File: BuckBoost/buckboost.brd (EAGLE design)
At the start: 100.1 x 80.4 mm, 10 parts

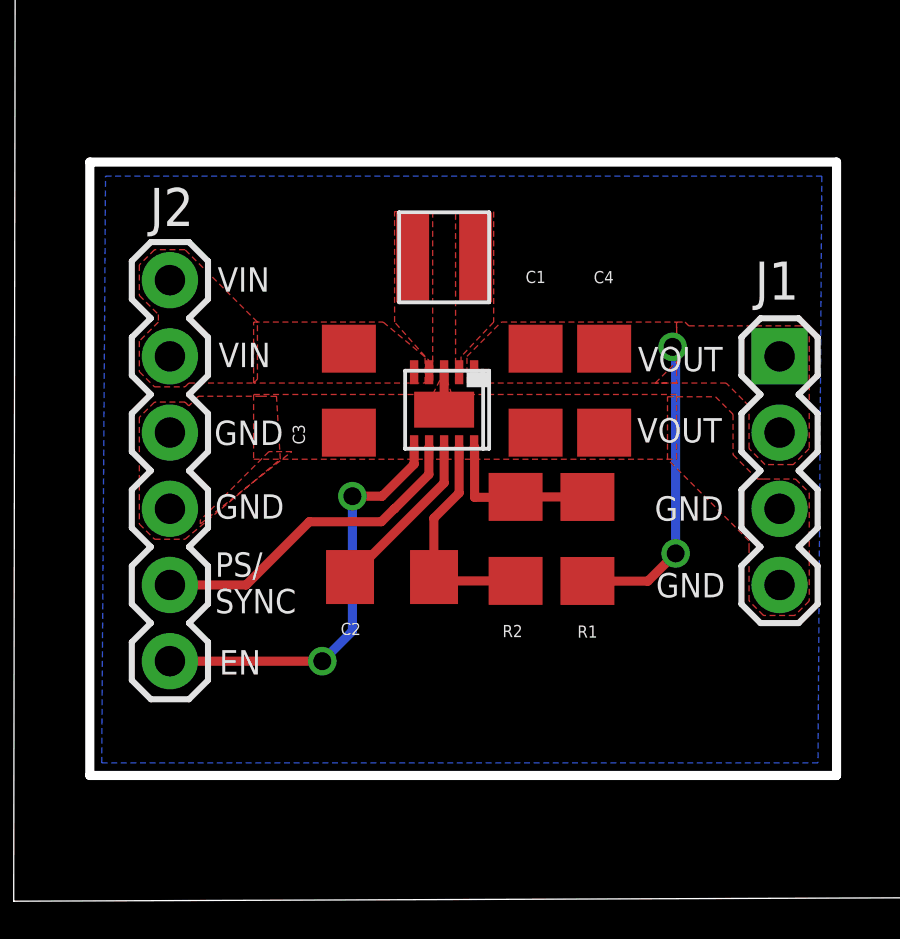
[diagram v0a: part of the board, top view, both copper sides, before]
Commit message: Added Jumpers
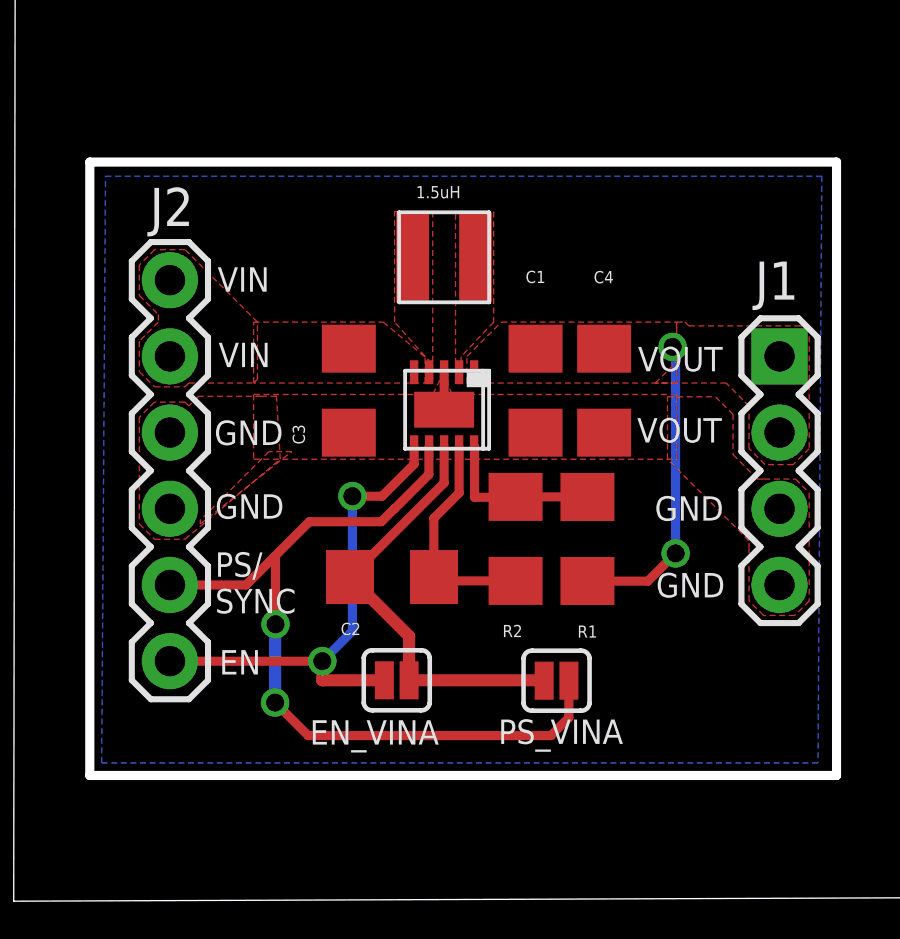
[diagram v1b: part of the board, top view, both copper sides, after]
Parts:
- added SJ1, SJ2: SOLDERJUMPERNC, SparkFun-Retired:SJ_2S
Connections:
- removed net N$2: J2.1, U$1.6
- new net N$5: J2.1, SJ1.1, U$1.6
- net N$3: now also SJ1.2, SJ2.1
- net N$4: now also SJ2.2
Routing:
- net N$5: track 0.00 -> 16.8 mm, vias 0 -> 2
- net N$4: track 11.1 -> 27.7 mm, vias 0 -> 2
- net N$2: track 14.1 -> 0.00 mm, vias 2 -> 0
- net N$3: track 5.63 -> 14.4 mm
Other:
- board text added: "1.5uH"
- board text added: "EN_VINA"
- board text added: "PS_VINA"
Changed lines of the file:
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@@
 <text x="21.236940625" y="12.303759375" size="0.8128" layer="21">GND</text>
 <text x="21.282659375" y="9.74598125" size="0.8128" layer="21">GND</text>
+<text x="9.743440625" y="4.8387" size="0.8128" layer="21">EN_VINA</text>
+<text x="16.024859375" y="4.861559375" size="0.8128" layer="21">PS_VINA</text>
+<text x="13.27911875" y="23.0505" size="0.4064" layer="21">1.5uH</text>
 </plain>
 <attributes>
@@
 <attribute name="VALUE" x="8.255" y="6.35" size="1.27" layer="27" rot="R90"/>
 </element>
+<element name="SJ1" library="SparkFun-Retired" package="SJ_2S" value="SOLDERJUMPERNC" x="12.64158125" y="6.982465625" smashed="yes"/>
+<element name="SJ2" library="SparkFun-Retired" package="SJ_2S" value="SOLDERJUMPERNC" x="17.9679625" y="6.969759375" smashed="yes"/>
 </elements>
 <signals>
@@
 <wire x1="14.22035625" y1="14.752" x2="14.22035625" y2="13.56035625" width="0.3048" layer="1"/>
 <wire x1="14.22035625" y1="13.56035625" x2="11.083778125" y2="10.423778125" width="0.3048" layer="1"/>
+<contactref element="SJ2" pad="1"/>
+<contactref element="SJ1" pad="2"/>
+<wire x1="13.05348125" y1="6.982465625" x2="13.05348125" y2="8.454075" width="0.4064" layer="1"/>
+<wire x1="13.05348125" y1="8.454075" x2="11.083778125" y2="10.423778125" width="0.4064" layer="1"/>
+<wire x1="13.05348125" y1="6.982465625" x2="17.54335625" y2="6.982465625" width="0.4064" layer="1"/>
+<wire x1="17.54335625" y1="6.982465625" x2="17.5560625" y2="6.969759375" width="0.4064" layer="1"/>
 </signal>
 <signal name="L2">
@@
 </polygon>
 </signal>
-<signal name="N$2">
+<signal name="N$4">
+<contactref element="U$1" pad="7"/>
+<wire x1="12.56935625" y1="12.7" x2="13.71235625" y2="13.843" width="0.3048" layer="1"/>
+<wire x1="13.71235625" y1="13.843" x2="13.71235625" y2="14.744" width="0.3048" layer="1"/>
+<wire x1="13.71235625" y1="14.744" x2="13.72035625" y2="14.752" width="0.3048" layer="1"/>
+<contactref element="J2" pad="2"/>
+<wire x1="5.08" y1="10.16" x2="7.62" y2="10.16" width="0.3048" layer="1"/>
+<wire x1="12.56935625" y1="12.7" x2="12.5603" y2="12.7" width="0.3048" layer="1"/>
+<wire x1="12.5603" y1="12.7" x2="12.1285" y2="12.2682" width="0.3048" layer="1"/>
+<wire x1="12.1285" y1="12.2682" x2="9.7282" y2="12.2682" width="0.3048" layer="1"/>
+<wire x1="9.7282" y1="12.2682" x2="8.569959375" y2="11.109959375" width="0.3048" layer="1"/>
+<contactref element="SJ2" pad="2"/>
+<via x="8.5877375" y="6.240778125" extent="1-16" drill="0.6" shape="square"/>
+<via x="8.60044375" y="8.849359375" extent="1-16" drill="0.6" shape="square"/>
+<wire x1="8.569959375" y1="11.109959375" x2="7.62" y2="10.16" width="0.3048" layer="1"/>
+<wire x1="8.5877375" y1="6.240778125" x2="8.5877375" y2="8.836653125" width="0.4064" layer="16"/>
+<wire x1="8.5877375" y1="8.836653125" x2="8.60044375" y2="8.849359375" width="0.4064" layer="16"/>
+<wire x1="8.60044375" y1="8.849359375" x2="8.60044375" y2="11.079475" width="0.3048" layer="1"/>
+<wire x1="8.60044375" y1="11.079475" x2="8.569959375" y2="11.109959375" width="0.3048" layer="1"/>
+<wire x1="18.3798625" y1="6.969759375" x2="18.3798625" y2="5.73828125" width="0.3048" layer="1"/>
+<wire x1="18.3798625" y1="5.73828125" x2="17.78" y2="5.13841875" width="0.3048" layer="1"/>
+<wire x1="17.78" y1="5.13841875" x2="9.690096875" y2="5.13841875" width="0.3048" layer="1"/>
+<wire x1="9.690096875" y1="5.13841875" x2="8.5877375" y2="6.240778125" width="0.3048" layer="1"/>
+</signal>
+<signal name="N$5">
+<contactref element="SJ1" pad="1"/>
 <contactref element="U$1" pad="6"/>
 <contactref element="J2" pad="1"/>
@@
 <via x="10.16" y="7.62" extent="1-16" drill="0.6" shape="square"/>
 <wire x1="10.16" y1="7.62" x2="5.08" y2="7.62" width="0.3048" layer="1"/>
-</signal>
-<signal name="N$4">
-<contactref element="U$1" pad="7"/>
-<wire x1="12.56935625" y1="12.7" x2="13.71235625" y2="13.843" width="0.3048" layer="1"/>
-<wire x1="13.71235625" y1="13.843" x2="13.71235625" y2="14.744" width="0.3048" layer="1"/>
-<wire x1="13.71235625" y1="14.744" x2="13.72035625" y2="14.752" width="0.3048" layer="1"/>
-<contactref element="J2" pad="2"/>
-<wire x1="5.08" y1="10.16" x2="7.62" y2="10.16" width="0.3048" layer="1"/>
-<wire x1="12.56935625" y1="12.7" x2="12.5603" y2="12.7" width="0.3048" layer="1"/>
-<wire x1="12.5603" y1="12.7" x2="12.1285" y2="12.2682" width="0.3048" layer="1"/>
-<wire x1="12.1285" y1="12.2682" x2="9.7282" y2="12.2682" width="0.3048" layer="1"/>
-<wire x1="9.7282" y1="12.2682" x2="7.62" y2="10.16" width="0.3048" layer="1"/>
+<wire x1="12.22968125" y1="6.982465625" x2="10.16" y2="6.982465625" width="0.4064" layer="1"/>
+<wire x1="10.16" y1="6.982465625" x2="10.16" y2="7.62" width="0.4064" layer="1"/>
 </signal>
 </signals>

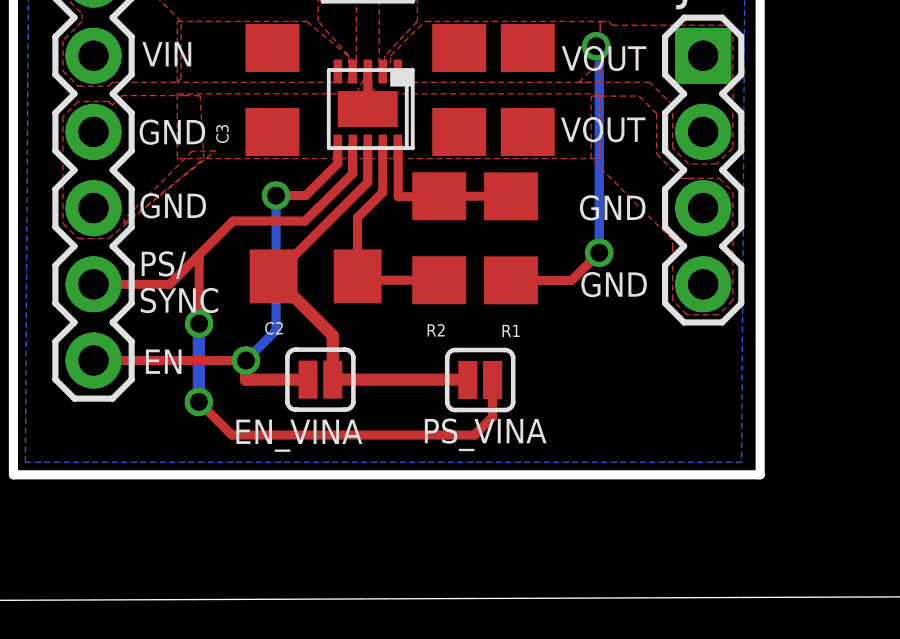
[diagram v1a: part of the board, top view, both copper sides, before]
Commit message: Added vout_vfb jumper
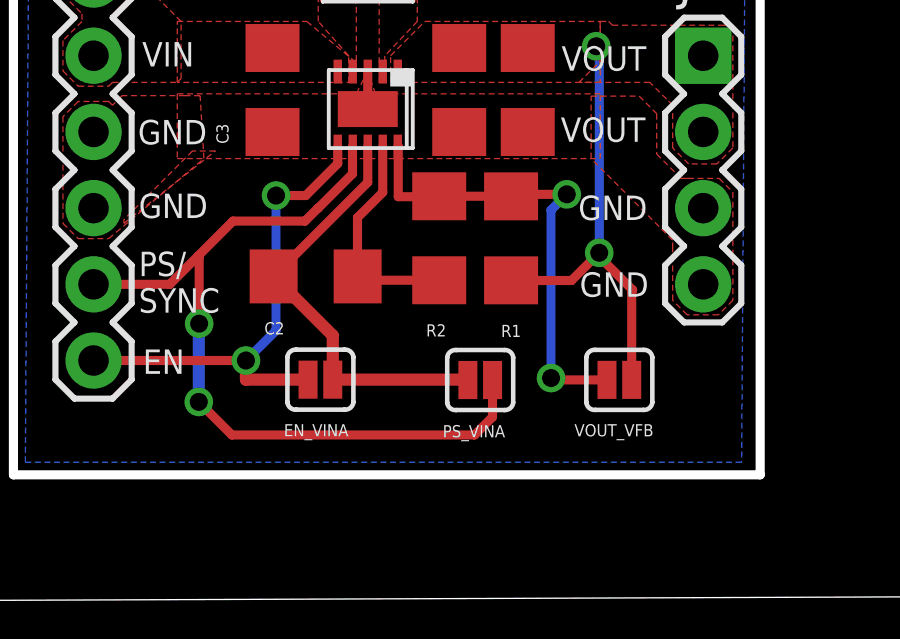
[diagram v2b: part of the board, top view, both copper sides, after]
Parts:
- added SJ3: SOLDERJUMPERNC, SparkFun-Retired:SJ_2S
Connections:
- net N$1: now also SJ3.1
- net VOUT: now also SJ3.2
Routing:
- net N$1: track 5.46 -> 15.6 mm, vias 0 -> 2
- net VOUT: track 10.3 -> 15.0 mm
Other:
- board text added: "VOUT_VFB"
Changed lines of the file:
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@@
 <text x="21.236940625" y="12.303759375" size="0.8128" layer="21">GND</text>
 <text x="21.282659375" y="9.74598125" size="0.8128" layer="21">GND</text>
-<text x="9.743440625" y="4.8387" size="0.8128" layer="21">EN_VINA</text>
-<text x="16.024859375" y="4.861559375" size="0.8128" layer="21">PS_VINA</text>
 <text x="13.27911875" y="23.0505" size="0.4064" layer="21">1.5uH</text>
+<text x="11.42491875" y="5.0927" size="0.4064" layer="21">EN_VINA</text>
+<text x="16.71828125" y="5.05968125" size="0.4064" layer="21">PS_VINA</text>
+<text x="21.1074" y="5.0927" size="0.4064" layer="21">VOUT_VFB</text>
 </plain>
 <attributes>
@@
 <element name="SJ1" library="SparkFun-Retired" package="SJ_2S" value="SOLDERJUMPERNC" x="12.64158125" y="6.982465625" smashed="yes"/>
 <element name="SJ2" library="SparkFun-Retired" package="SJ_2S" value="SOLDERJUMPERNC" x="17.9679625" y="6.969759375" smashed="yes"/>
+<element name="SJ3" library="SparkFun-Retired" package="SJ_2S" value="SOLDERJUMPERNC" x="22.606" y="6.974840625" smashed="yes"/>
 </elements>
 <signals>
@@
 <wire x1="21.93678125" y1="11.211690625" x2="21.93678125" y2="17.9960375" width="0.3048" layer="16"/>
 <wire x1="21.93678125" y1="17.9960375" x2="21.8369375" y2="18.09588125" width="0.3048" layer="16"/>
+<contactref element="SJ3" pad="2"/>
+<wire x1="23.05091875" y1="9.96908125" x2="21.93678125" y2="11.08321875" width="0.3048" layer="1"/>
+<wire x1="21.93678125" y1="11.08321875" x2="21.93678125" y2="11.211690625" width="0.3048" layer="1"/>
+<wire x1="23.05091875" y1="9.96908125" x2="23.0179" y2="9.9360625" width="0.3048" layer="1"/>
+<wire x1="23.0179" y1="9.9360625" x2="23.0179" y2="6.974840625" width="0.3048" layer="1"/>
 </signal>
 <signal name="N$1">
@@
 <wire x1="15.23635625" y1="13.081" x2="16.60293125" y2="13.081" width="0.3048" layer="1"/>
 <wire x1="16.60293125" y1="13.081" x2="16.60293125" y2="13.0957" width="0.3048" layer="1"/>
+<contactref element="SJ3" pad="1"/>
+<wire x1="18.99775625" y1="13.0930875" x2="19.064409375" y2="13.159740625" width="0.3048" layer="1"/>
+<wire x1="19.064409375" y1="13.159740625" x2="20.8534" y2="13.159740625" width="0.3048" layer="1"/>
+<via x="20.8534" y="13.159740625" extent="1-16" drill="0.6" shape="square"/>
+<wire x1="20.8534" y1="13.159740625" x2="20.330159375" y2="12.6365" width="0.3048" layer="16"/>
+<wire x1="20.330159375" y1="12.6365" x2="20.330159375" y2="7.0358" width="0.3048" layer="16"/>
+<via x="20.330159375" y="7.0358" extent="1-16" drill="0.6" shape="square"/>
+<wire x1="20.330159375" y1="7.0358" x2="20.39111875" y2="6.974840625" width="0.3048" layer="1"/>
+<wire x1="20.39111875" y1="6.974840625" x2="22.1941" y2="6.974840625" width="0.3048" layer="1"/>
 </signal>
 <signal name="GND">

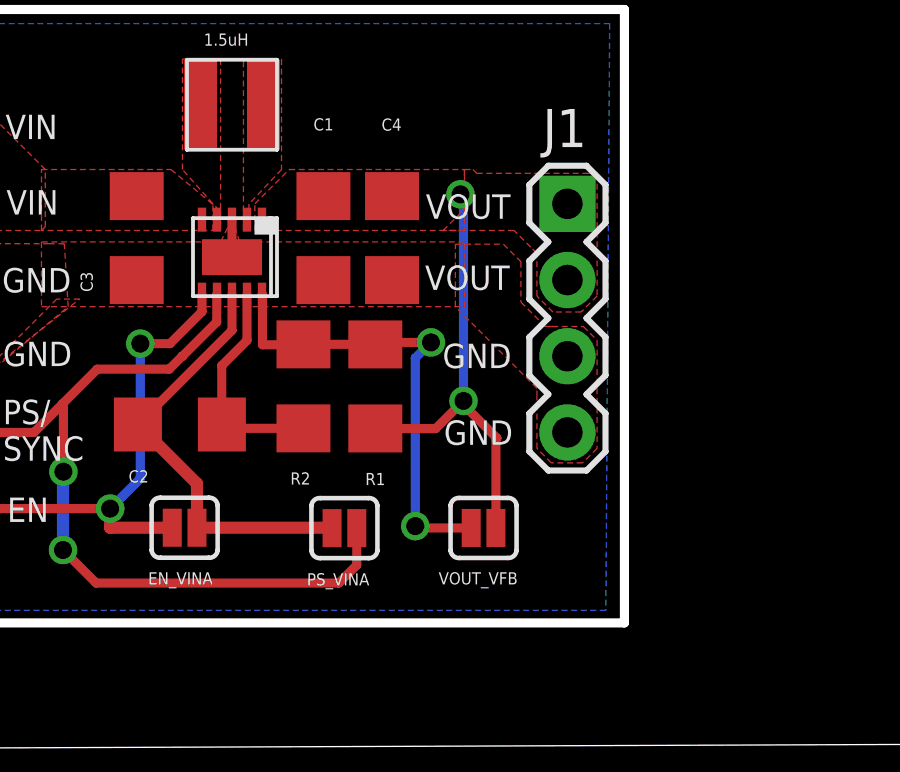
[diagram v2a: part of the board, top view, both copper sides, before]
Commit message: moved fb_vout jumper
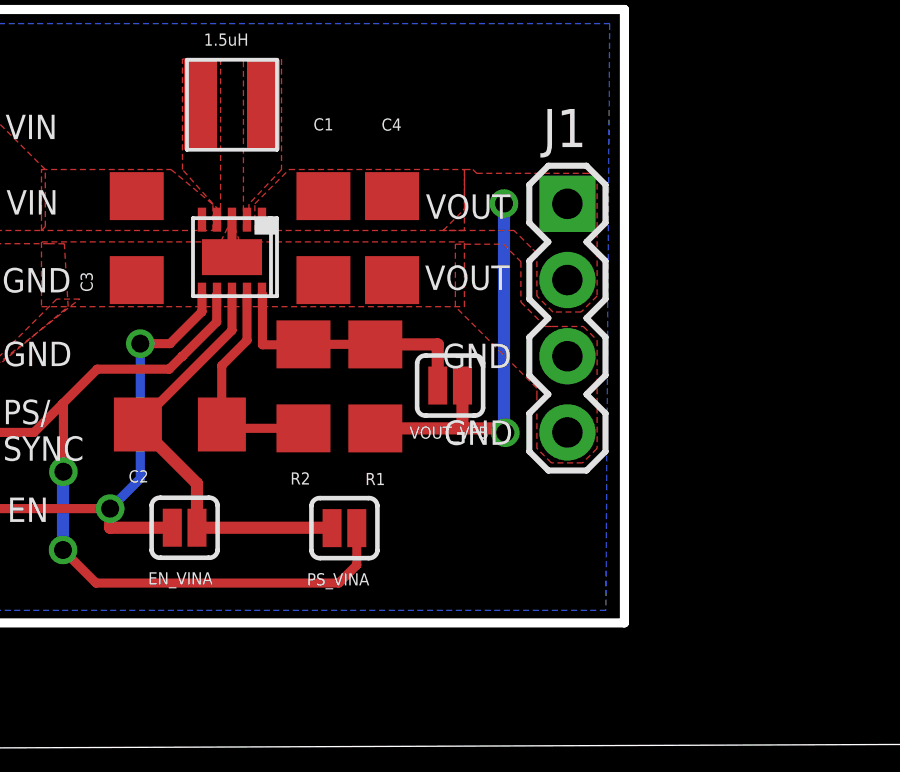
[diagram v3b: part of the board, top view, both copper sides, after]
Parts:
- moved SJ3 4.88 mm to (21.5, 11.7)
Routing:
- net N$1: track 15.6 -> 9.01 mm, vias 2 -> 0
- net VOUT: track 15.0 -> 13.6 mm
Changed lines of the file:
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@@
 <text x="11.42491875" y="5.0927" size="0.4064" layer="21">EN_VINA</text>
 <text x="16.71828125" y="5.05968125" size="0.4064" layer="21">PS_VINA</text>
-<text x="21.1074" y="5.0927" size="0.4064" layer="21">VOUT_VFB</text>
+<text x="20.13711875" y="9.94918125" size="0.4064" layer="21">VOUT_VFB</text>
 </plain>
 <attributes>
@@
 <element name="SJ1" library="SparkFun-Retired" package="SJ_2S" value="SOLDERJUMPERNC" x="12.64158125" y="6.982465625" smashed="yes"/>
 <element name="SJ2" library="SparkFun-Retired" package="SJ_2S" value="SOLDERJUMPERNC" x="17.9679625" y="6.969759375" smashed="yes"/>
-<element name="SJ3" library="SparkFun-Retired" package="SJ_2S" value="SOLDERJUMPERNC" x="22.606" y="6.974840625" smashed="yes"/>
+<element name="SJ3" library="SparkFun-Retired" package="SJ_2S" value="SOLDERJUMPERNC" x="21.490940625" y="11.7221" smashed="yes"/>
 </elements>
 <signals>
@@
 <contactref element="C4" pad="1"/>
 <contactref element="R1" pad="1"/>
-<via x="21.93678125" y="11.211690625" extent="1-16" drill="0.6" shape="square"/>
-<via x="21.8369375" y="18.09588125" extent="1-16" drill="0.6" shape="square"/>
+<via x="23.331240625" y="10.149971875" extent="1-16" drill="0.6" shape="square"/>
+<via x="23.287275" y="17.788540625" extent="1-16" drill="0.6" shape="square"/>
 <polygon width="0.3048" layer="1" thermals="no" rank="2">
 <vertex x="21.96735625" y="16.891"/>
@@
 <contactref element="J1" pad="1"/>
 <contactref element="J1" pad="2"/>
-<wire x1="18.99775625" y1="10.287" x2="21.012090625" y2="10.287" width="0.3048" layer="1"/>
-<wire x1="21.012090625" y1="10.287" x2="21.93678125" y2="11.211690625" width="0.3048" layer="1"/>
-<wire x1="21.93678125" y1="11.211690625" x2="21.93678125" y2="17.9960375" width="0.3048" layer="16"/>
-<wire x1="21.93678125" y1="17.9960375" x2="21.8369375" y2="18.09588125" width="0.3048" layer="16"/>
 <contactref element="SJ3" pad="2"/>
-<wire x1="23.05091875" y1="9.96908125" x2="21.93678125" y2="11.08321875" width="0.3048" layer="1"/>
-<wire x1="21.93678125" y1="11.08321875" x2="21.93678125" y2="11.211690625" width="0.3048" layer="1"/>
-<wire x1="23.05091875" y1="9.96908125" x2="23.0179" y2="9.9360625" width="0.3048" layer="1"/>
-<wire x1="23.0179" y1="9.9360625" x2="23.0179" y2="6.974840625" width="0.3048" layer="1"/>
+<wire x1="23.331240625" y1="10.149971875" x2="23.287275" y2="10.149971875" width="0.4064" layer="16"/>
+<wire x1="23.287275" y1="10.149971875" x2="23.287275" y2="17.788540625" width="0.4064" layer="16"/>
+<wire x1="18.99775625" y1="10.2930875" x2="21.902840625" y2="10.2930875" width="0.4064" layer="1"/>
+<wire x1="23.331240625" y1="10.2930875" x2="23.331240625" y2="10.149971875" width="0.4064" layer="1"/>
+<wire x1="23.331240625" y1="10.2930875" x2="21.902840625" y2="10.2930875" width="0.4064" layer="1"/>
+<wire x1="21.902840625" y1="10.2930875" x2="21.902840625" y2="11.7221" width="0.4064" layer="1"/>
 </signal>
 <signal name="N$1">
@@
 <contactref element="SJ3" pad="1"/>
 <wire x1="18.99775625" y1="13.0930875" x2="19.064409375" y2="13.159740625" width="0.3048" layer="1"/>
-<wire x1="19.064409375" y1="13.159740625" x2="20.8534" y2="13.159740625" width="0.3048" layer="1"/>
-<via x="20.8534" y="13.159740625" extent="1-16" drill="0.6" shape="square"/>
-<wire x1="20.8534" y1="13.159740625" x2="20.330159375" y2="12.6365" width="0.3048" layer="16"/>
-<wire x1="20.330159375" y1="12.6365" x2="20.330159375" y2="7.0358" width="0.3048" layer="16"/>
-<via x="20.330159375" y="7.0358" extent="1-16" drill="0.6" shape="square"/>
-<wire x1="20.330159375" y1="7.0358" x2="20.39111875" y2="6.974840625" width="0.3048" layer="1"/>
-<wire x1="20.39111875" y1="6.974840625" x2="22.1941" y2="6.974840625" width="0.3048" layer="1"/>
+<wire x1="21.079040625" y1="11.7221" x2="21.079040625" y2="13.0930875" width="0.4064" layer="1"/>
+<wire x1="21.079040625" y1="13.0930875" x2="18.99775625" y2="13.0930875" width="0.4064" layer="1"/>
 </signal>
 <signal name="GND">
